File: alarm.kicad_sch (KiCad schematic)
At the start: 0 parts

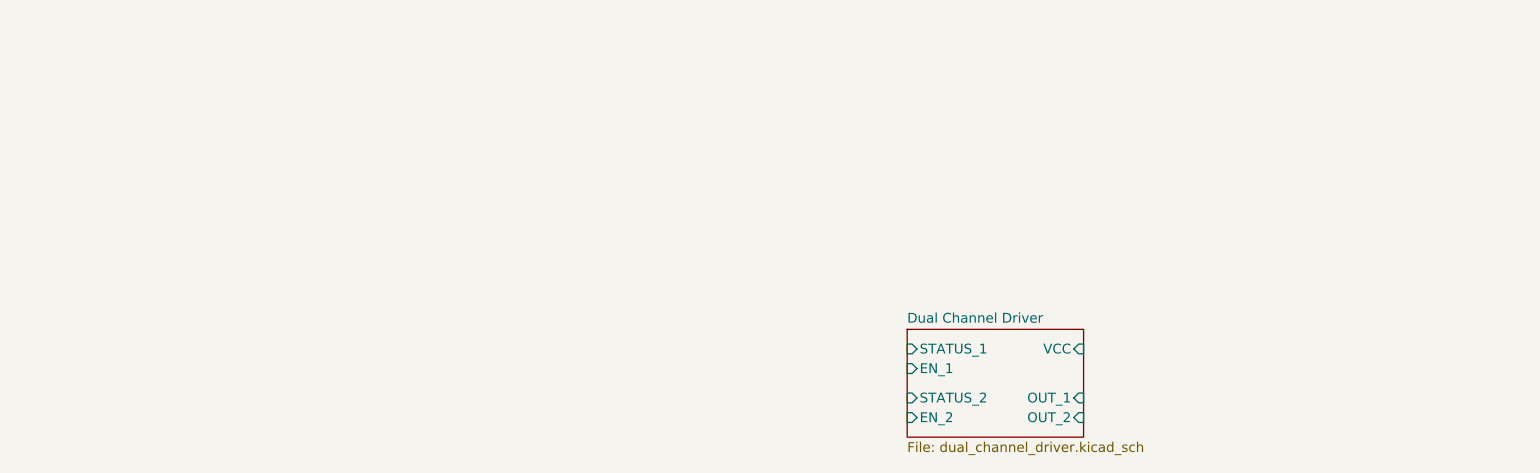
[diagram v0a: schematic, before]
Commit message: add mic2940a
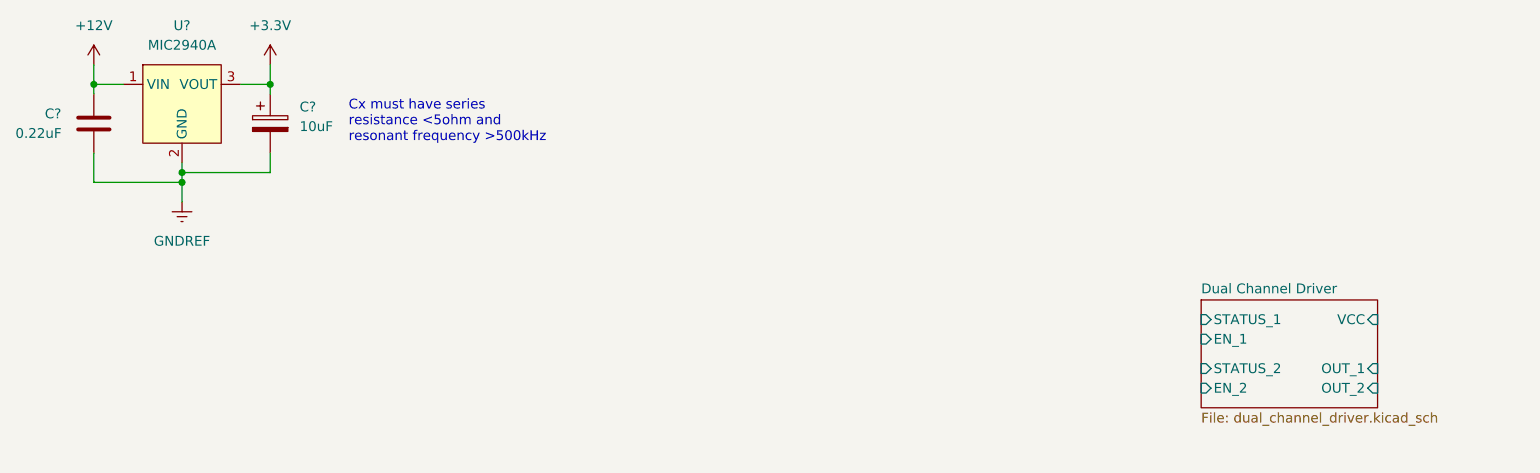
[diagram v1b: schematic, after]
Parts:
- added C?: 10uF, symbol Device:C_Polarized
- added C?: 0.22uF, Capacitor_SMD:C_0805_2012Metric_Pad1.18x1.45mm_HandSolder, symbol Device:C
- added U?: MIC2940A, Package_TO_SOT_SMD:TO-263-3_TabPin4, symbol mic2940a:MIC2940A
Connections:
- new net +12V: C?.2, U?.1 (VIN)
- new net +3.3V: C?.1, U?.3 (VOUT)
- new net GNDREF: C?.1, C?.2, U?.2 (GND)
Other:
- note added: "Cx must have series resistance <5ohm and resonant frequency >500kHz"
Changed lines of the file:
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@@
 (kicad_sch (version 20211123) (generator eeschema)
   (paper "A4")
-  (sheet (at 142.24 72.39) (size 22.86 13.97) (fields_autoplaced)
+  (junction (at 36.83 40.64) (diameter 0) (color 0 0 0 0)
+  )
+  (junction (at 48.26 52.07) (diameter 0) (color 0 0 0 0)
+  )
+  (junction (at 48.26 53.34) (diameter 0) (color 0 0 0 0)
+  )
+  (junction (at 59.69 40.64) (diameter 0) (color 0 0 0 0)
+  )
+  (wire (pts (xy 36.83 53.34) (xy 48.26 53.34))
+    (stroke (width 0) (type default) (color 0 0 0 0))
+  )
+  (wire (pts (xy 36.83 49.53) (xy 36.83 53.34))
+    (stroke (width 0) (type default) (color 0 0 0 0))
+  )
+  (wire (pts (xy 59.69 41.91) (xy 59.69 40.64))
+    (stroke (width 0) (type default) (color 0 0 0 0))
+  )
+  (wire (pts (xy 48.26 52.07) (xy 59.69 52.07))
+    (stroke (width 0) (type default) (color 0 0 0 0))
+  )
+  (wire (pts (xy 59.69 40.64) (xy 55.88 40.64))
+    (stroke (width 0) (type default) (color 0 0 0 0))
+  )
+  (wire (pts (xy 59.69 38.1) (xy 59.69 40.64))
+    (stroke (width 0) (type default) (color 0 0 0 0))
+  )
+  (wire (pts (xy 36.83 40.64) (xy 36.83 41.91))
+    (stroke (width 0) (type default) (color 0 0 0 0))
+  )
+  (wire (pts (xy 36.83 40.64) (xy 40.64 40.64))
+    (stroke (width 0) (type default) (color 0 0 0 0))
+  )
+  (wire (pts (xy 48.26 53.34) (xy 48.26 55.88))
+    (stroke (width 0) (type default) (color 0 0 0 0))
+  )
+  (wire (pts (xy 59.69 52.07) (xy 59.69 49.53))
+    (stroke (width 0) (type default) (color 0 0 0 0))
+  )
+  (wire (pts (xy 48.26 52.07) (xy 48.26 53.34))
+    (stroke (width 0) (type default) (color 0 0 0 0))
+  )
+  (wire (pts (xy 48.26 50.8) (xy 48.26 52.07))
+    (stroke (width 0) (type default) (color 0 0 0 0))
+  )
+  (wire (pts (xy 36.83 38.1) (xy 36.83 40.64))
+    (stroke (width 0) (type default) (color 0 0 0 0))
+  )
+  (text "Cx must have series \nresistance <5ohm and\nresonant frequency >500kHz"
+    (at 69.85 48.26 0)
+    (effects (font (size 1.27 1.27)) (justify left bottom))
+  )
+  (symbol (lib_id "Device:C_Polarized") (at 59.69 45.72 0) (unit 1)
+    (in_bom yes) (on_board yes) (fields_autoplaced)
+    (property "Reference" "C?" (id 0) (at 63.5 43.5609 0)
+      (effects (font (size 1.27 1.27)) (justify left))
+    )
+    (property "Value" "10uF" (id 1) (at 63.5 46.1009 0)
+      (effects (font (size 1.27 1.27)) (justify left))
+    )
+    (property "Footprint" "" (id 2) (at 60.6552 49.53 0)
+      (effects (font (size 1.27 1.27)) hide)
+    )
+    (property "Datasheet" "~" (id 3) (at 59.69 45.72 0)
+      (effects (font (size 1.27 1.27)) hide)
+    )
+    (pin "1")
+    (pin "2")
+  )
+  (symbol (lib_id "power:GNDREF") (at 48.26 55.88 0) (unit 1)
+    (in_bom yes) (on_board yes) (fields_autoplaced)
+    (property "Reference" "#PWR?" (id 0) (at 48.26 62.23 0)
+      (effects (font (size 1.27 1.27)) hide)
+    )
+    (property "Value" "GNDREF" (id 1) (at 48.26 60.96 0))
+    (property "Footprint" "" (id 2) (at 48.26 55.88 0)
+      (effects (font (size 1.27 1.27)) hide)
+    )
+    (property "Datasheet" "" (id 3) (at 48.26 55.88 0)
+      (effects (font (size 1.27 1.27)) hide)
+    )
+    (pin "1")
+  )
+  (symbol (lib_id "power:+3.3V") (at 59.69 38.1 0) (unit 1)
+    (in_bom yes) (on_board yes) (fields_autoplaced)
+    (property "Reference" "#PWR?" (id 0) (at 59.69 41.91 0)
+      (effects (font (size 1.27 1.27)) hide)
+    )
+    (property "Value" "+3.3V" (id 1) (at 59.69 33.02 0))
+    (property "Footprint" "" (id 2) (at 59.69 38.1 0)
+      (effects (font (size 1.27 1.27)) hide)
+    )
+    (property "Datasheet" "" (id 3) (at 59.69 38.1 0)
+      (effects (font (size 1.27 1.27)) hide)
+    )
+    (pin "1")
+  )
+  (symbol (lib_id "power:+12V") (at 36.83 38.1 0) (unit 1)
+    (in_bom yes) (on_board yes) (fields_autoplaced)
+    (property "Reference" "#PWR?" (id 0) (at 36.83 41.91 0)
+      (effects (font (size 1.27 1.27)) hide)
+    )
+    (property "Value" "+12V" (id 1) (at 36.83 33.02 0))
+    (property "Footprint" "" (id 2) (at 36.83 38.1 0)
+      (effects (font (size 1.27 1.27)) hide)
+    )
+    (property "Datasheet" "" (id 3) (at 36.83 38.1 0)
+      (effects (font (size 1.27 1.27)) hide)
+    )
+    (pin "1")
+  )
+  (symbol (lib_id "mic2940a:MIC2940A") (at 48.26 43.18 0) (unit 1)
+    (in_bom yes) (on_board yes) (fields_autoplaced)
+    (property "Reference" "U?" (id 0) (at 48.26 33.02 0))
+    (property "Value" "MIC2940A" (id 1) (at 48.26 35.56 0))
+    (property "Footprint" "Package_TO_SOT_SMD:TO-263-3_TabPin4" (id 2) (at 48.26 35.56 0)
+      (effects (font (size 1.27 1.27)) hide)
+    )
+    (property "Datasheet" "https://ww1.microchip.com/downloads/en/DeviceDoc/MIC2940A-41A-1-25A-Low-Dropout-Regulator-DS20006000A.pdf" (id 3) (at 48.26 35.56 0)
+      (effects (font (size 1.27 1.27)) hide)
+    )
+    (pin "1")
+    (pin "2")
+    (pin "3")
+  )
+  (symbol (lib_id "Device:C") (at 36.83 45.72 180) (unit 1)
+    (in_bom yes) (on_board yes)
+    (property "Reference" "C?" (id 0) (at 30.48 44.45 0)
+      (effects (font (size 1.27 1.27)) (justify right))
+    )
+    (property "Value" "0.22uF" (id 1) (at 26.67 46.99 0)
+      (effects (font (size 1.27 1.27)) (justify right))
+    )
+    (property "Footprint" "Capacitor_SMD:C_0805_2012Metric_Pad1.18x1.45mm_HandSolder" (id 2) (at 35.8648 41.91 0)
+      (effects (font (size 1.27 1.27)) hide)
+    )
+    (property "Datasheet" "~" (id 3) (at 36.83 45.72 0)
+      (effects (font (size 1.27 1.27)) hide)
+    )
+    (pin "1")
+    (pin "2")
+  )
+  (sheet (at 180.34 68.58) (size 22.86 13.97) (fields_autoplaced)
     (stroke (width 0.1524) (type solid) (color 0 0 0 0))
     (fill (color 0 0 0 0.0000))
-    (property "Sheet name" "Dual Channel Driver" (id 0) (at 142.24 71.6784 0)
+    (property "Sheet name" "Dual Channel Driver" (id 0) (at 180.34 67.8684 0)
       (effects (font (size 1.27 1.27)) (justify left bottom))
     )
-    (property "Sheet file" "dual_channel_driver.kicad_sch" (id 1) (at 142.24 86.9446 0)
+    (property "Sheet file" "dual_channel_driver.kicad_sch" (id 1) (at 180.34 83.1346 0)
       (effects (font (size 1.27 1.27)) (justify left top))
     )
-    (pin "EN_2" input (at 142.24 83.82 180)
-      (effects (font (size 1.27 1.27)) (justify left))
-    )
-    (pin "STATUS_2" input (at 142.24 81.28 180)
-      (effects (font (size 1.27 1.27)) (justify left))
-    )
-    (pin "VCC" input (at 165.1 74.93 0)
-      (effects (font (size 1.27 1.27)) (justify right))
-    )
-    (pin "OUT_1" input (at 165.1 81.28 0)
-      (effects (font (size 1.27 1.27)) (justify right))
-    )
-    (pin "OUT_2" input (at 165.1 83.82 0)
-      (effects (font (size 1.27 1.27)) (justify right))
-    )
-    (pin "EN_1" input (at 142.24 77.47 180)
-      (effects (font (size 1.27 1.27)) (justify left))
-    )
-    (pin "STATUS_1" input (at 142.24 74.93 180)
+    (pin "EN_2" input (at 180.34 80.01 180)
+      (effects (font (size 1.27 1.27)) (justify left))
+    )
+    (pin "STATUS_2" input (at 180.34 77.47 180)
+      (effects (font (size 1.27 1.27)) (justify left))
+    )
+    (pin "VCC" input (at 203.2 71.12 0)
+      (effects (font (size 1.27 1.27)) (justify right))
+    )
+    (pin "OUT_1" input (at 203.2 77.47 0)
+      (effects (font (size 1.27 1.27)) (justify right))
+    )
+    (pin "OUT_2" input (at 203.2 80.01 0)
+      (effects (font (size 1.27 1.27)) (justify right))
+    )
+    (pin "EN_1" input (at 180.34 73.66 180)
+      (effects (font (size 1.27 1.27)) (justify left))
+    )
+    (pin "STATUS_1" input (at 180.34 71.12 180)
       (effects (font (size 1.27 1.27)) (justify left))
     )
@@
       (reference "#PWR0101") (unit 1) (value "GNDREF") (footprint "")
     )
+    (path "/43c5c993-1aae-4740-9815-63353f540617"
+      (reference "#PWR?") (unit 1) (value "GNDREF") (footprint "")
+    )
+    (path "/62511bc9-1f05-4453-842f-32adaa780cbf"
+      (reference "#PWR?") (unit 1) (value "+3.3V") (footprint "")
+    )
+    (path "/8ffe4b20-985e-4198-81ef-01757e4202e9"
+      (reference "#PWR?") (unit 1) (value "+12V") (footprint "")
+    )
+    (path "/39650689-3121-43c1-b4c2-e8b04f296adb"
+      (reference "C?") (unit 1) (value "10uF") (footprint "")
+    )
+    (path "/d89c7d32-659f-4b13-b4be-70f941917c9d"
+      (reference "C?") (unit 1) (value "0.22uF") (footprint "Capacitor_SMD:C_0805_2012Metric_Pad1.18x1.45mm_HandSolder")
+    )
     (path "/d7765555-85d1-40ab-a055-81354f0195d8/7a6862c2-08e6-4d59-8269-e264db8e7deb"
       (reference "R1") (unit 1) (value "10k") (footprint "Resistor_SMD:R_0805_2012Metric_Pad1.20x1.40mm_HandSolder")
@@
       (reference "U1") (unit 3) (value "VND5160J") (footprint "PowerSSO:POWERSSO-12")
     )
-  )
+    (path "/c2dfd7f9-510d-4fb0-a55a-3cb1265470e3"
+      (reference "U?") (unit 1) (value "MIC2940A") (footprint "Package_TO_SOT_SMD:TO-263-3_TabPin4")
+    )
+  )
